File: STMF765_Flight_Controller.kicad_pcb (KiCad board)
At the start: 4 copper layers, 40 x 40 mm, 231 parts, among them J1 10155435-00011LF, SW1 SW_Push, U1 STM32F765VITx, U10 ESDS304DBVR, U11 ESD351DPYR, U12 ATtiny25-20SS, U13 TJA1051TK-3, U14 TJA1051TK-3, U2 AT7456E, U3 TXU0304PWR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

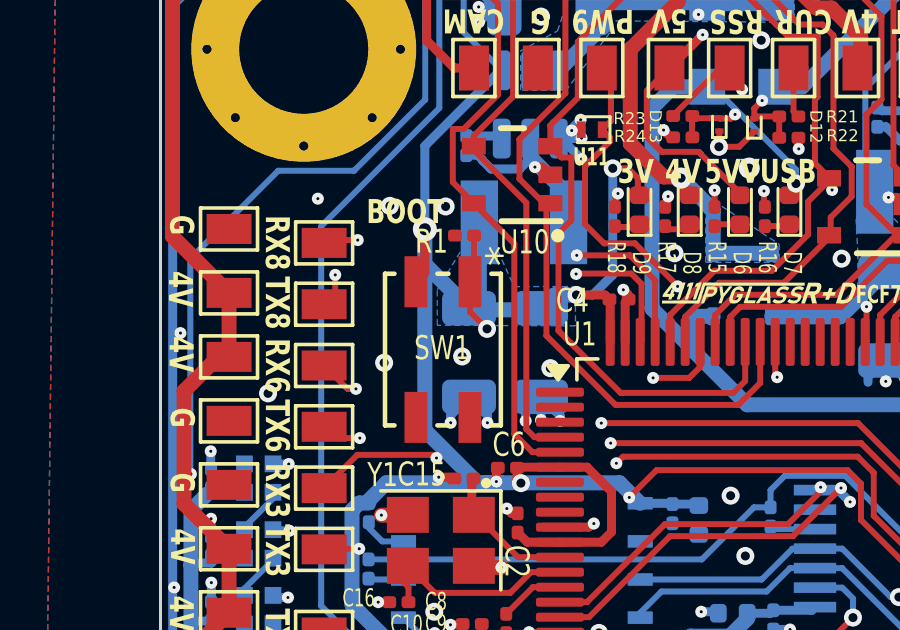
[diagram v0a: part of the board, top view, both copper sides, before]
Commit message: use smaller button
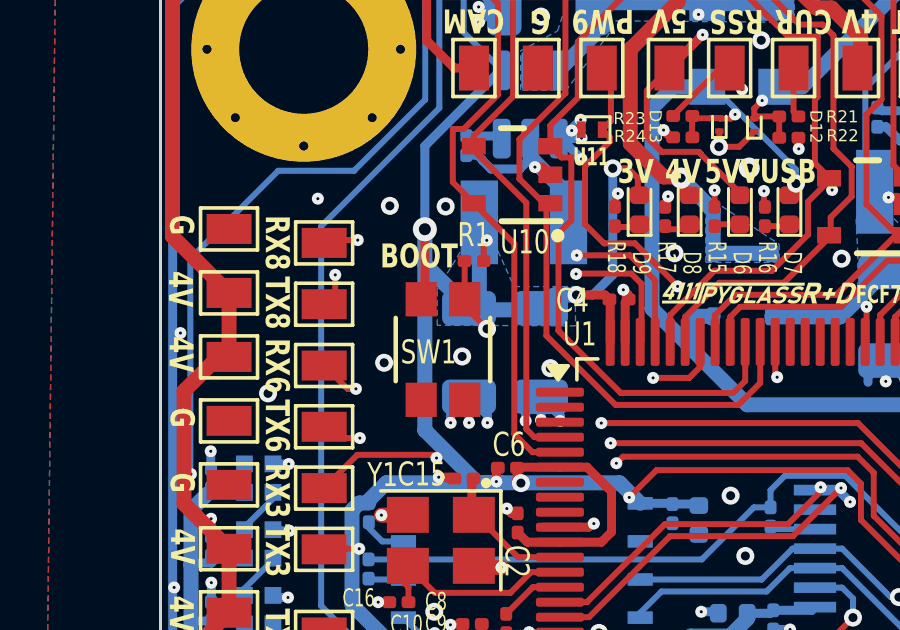
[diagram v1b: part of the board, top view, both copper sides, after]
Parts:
- R15, R16: value 3k3 -> 1k5
- R17: value 3k3 -> 1k2
- R18, R29: value 1k2 -> 680
- R21: value 22k1 -> 0
- R22: value 3k3 -> 10M
- R23: value 3k3 -> 0
- SW1: footprint Project:SWITCH_EVQP2_PAN -> Project:EVPAA602
- moved R1 0.91 mm to (160.3, 62.1), turned to 0 degrees
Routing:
- net Net-(U1-BOOT0): track 12.2 -> 11.3 mm
- net GND: track 116.1 -> 116.8 mm, vias 184 -> 185
- net +3V3: track 355.2 -> 355.7 mm

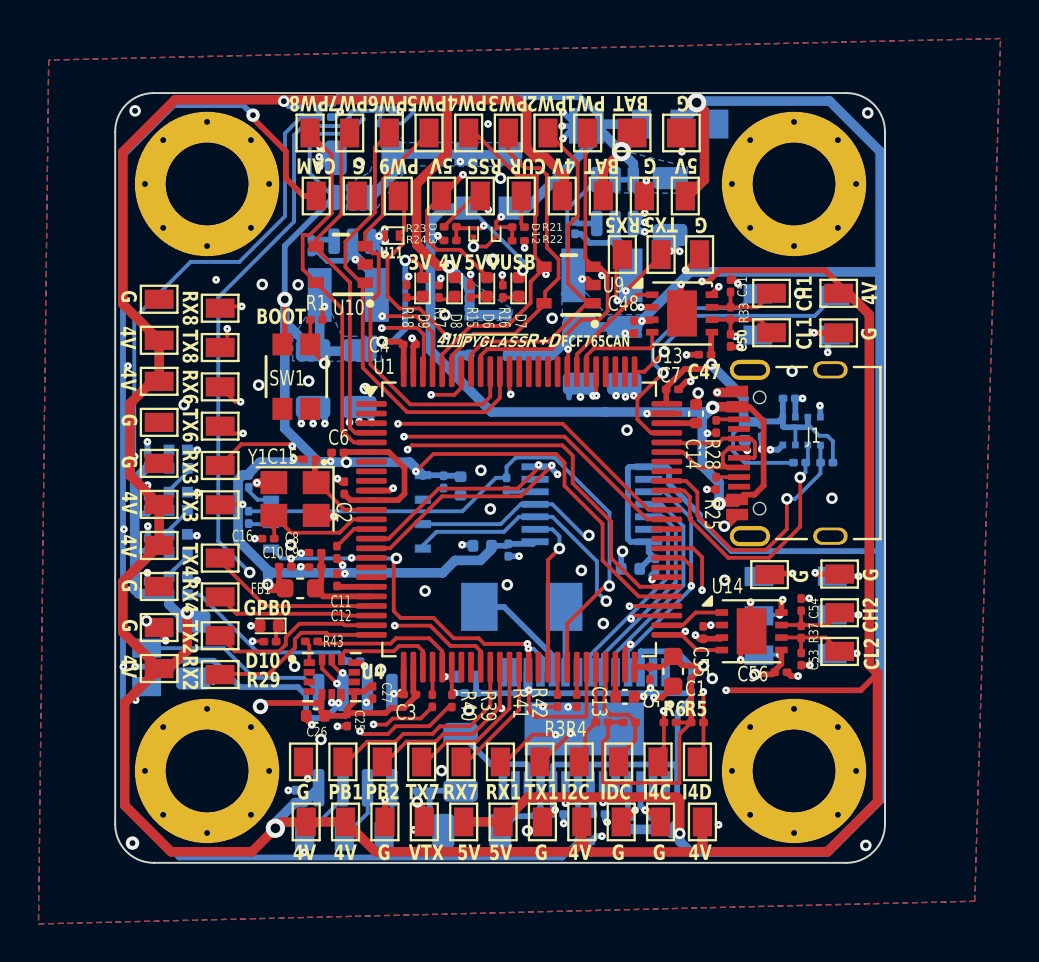
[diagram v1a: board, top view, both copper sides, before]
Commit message: remove microvias, still need to update silkmasks
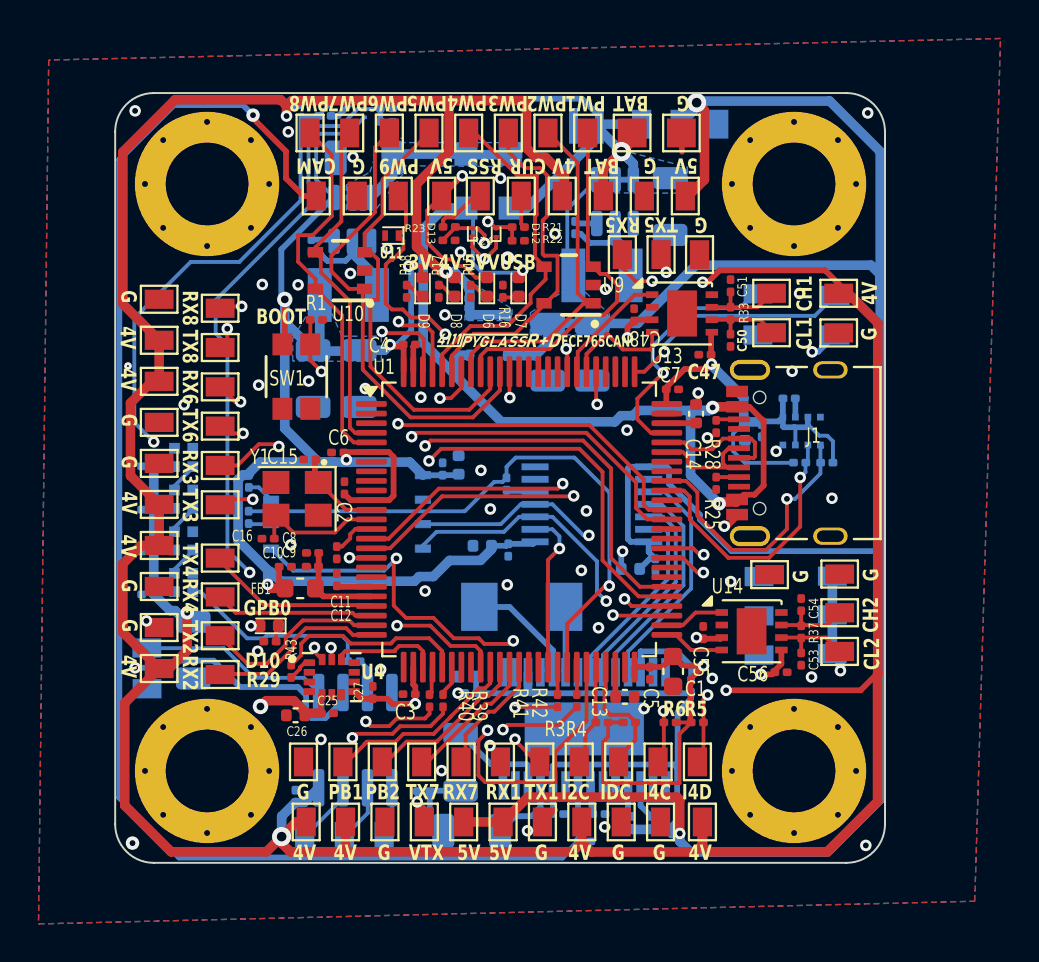
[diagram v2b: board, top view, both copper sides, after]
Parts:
- moved R43 1.88 mm to (159.0, 80.3), turned to 90 degrees
- moved C35 1.69 mm to (172.3, 63.7)
- moved C36 1.68 mm to (174.6, 63.7)
- moved C29 1.09 mm to (167.7, 69.6), turned to 90 degrees
- moved C25 1.09 mm to (160.8, 82.5), turned to 0 degrees
- moved C26 1.03 mm to (159.2, 82.6)
- moved R31 0.81 mm to (160.7, 50.7), turned to 180 degrees
- moved R19 0.78 mm to (163.9, 51.1)
- moved R30 0.68 mm to (160.7, 51.5)
- moved C28 0.67 mm to (166.8, 69.8), turned to 90 degrees
- moved R20 0.65 mm to (163.9, 51.8)
- moved C48 0.64 mm to (176.8, 61.8), turned to -90 degrees
- moved R39 0.46 mm to (166.9, 81.8)
- moved C42 0.36 mm to (151.5, 74.1), turned to 180 degrees
- moved C43 0.36 mm to (151.5, 71.9), turned to 180 degrees
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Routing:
- net GND: track 116.8 -> 22.5 mm, vias 185 -> 51
- net SPI4_CS_FLASH: track 26.3 -> 35.4 mm
- net SPI4_MOSI: track 19.8 -> 27.3 mm
- net +3V3: track 355.7 -> 362.2 mm, vias 14 -> 13
- net ADC1_IN2_RSS: track 28.1 -> 32.7 mm
- net ADC1_IN1_A: track 28.8 -> 33.3 mm
- net +4V: track 208.1 -> 212.6 mm
- net USART1_TX: track 11.3 -> 15.6 mm
- net USART1_RX: track 13.5 -> 16.9 mm
- net VBUS: track 47.0 -> 50.2 mm
- net SPI1_MISO: track 7.73 -> 10.2 mm
- net SPI1_SCK: track 7.97 -> 10.3 mm
- net SPI4_SCK: track 20.4 -> 22.5 mm
- net SPI1_MOSI: track 9.95 -> 11.9 mm
- net UART5_TX: track 10.1 -> 11.8 mm
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
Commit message: adjust silk screens after microvia replacement
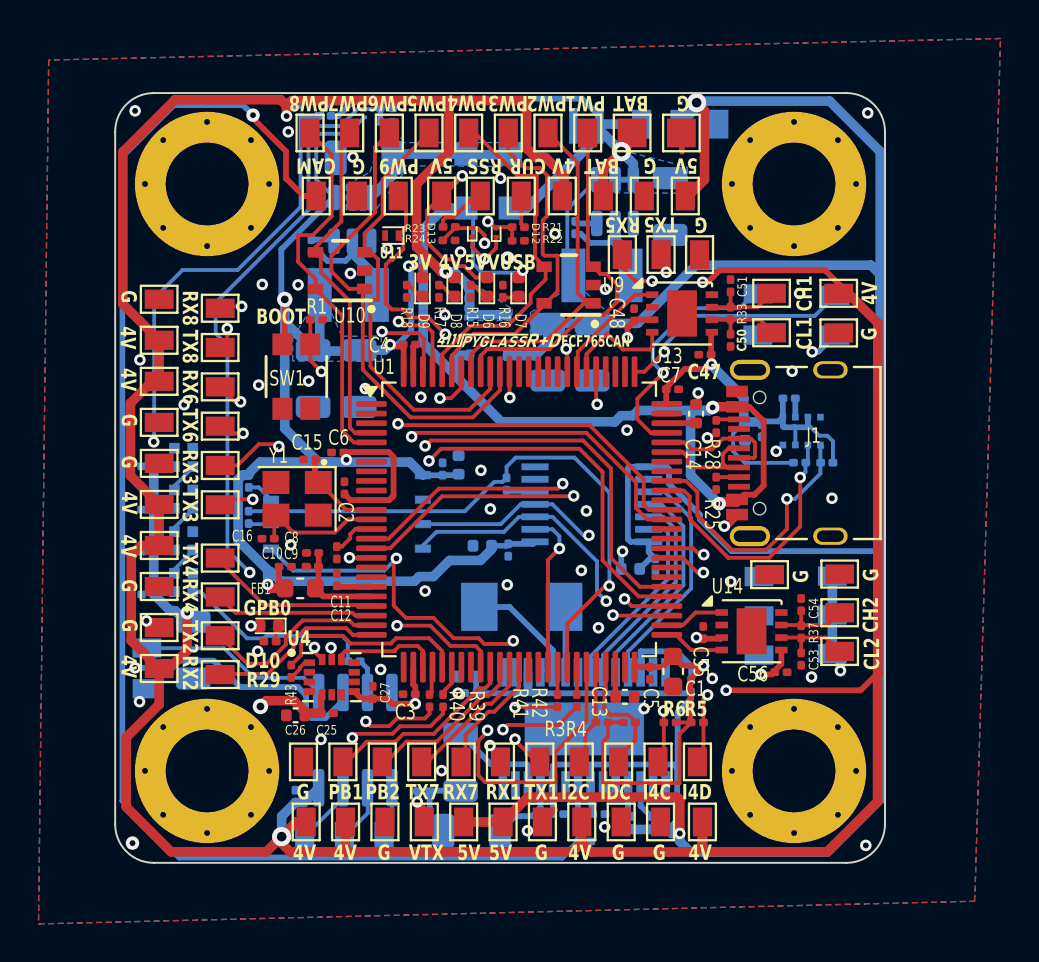
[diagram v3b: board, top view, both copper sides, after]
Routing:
- net /Power Monitor/ADC: track 50.2 -> 49.5 mm
- net GND: vias 51 -> 52

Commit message: change flash to sd flash, cleanup, and reconcile with F405FC
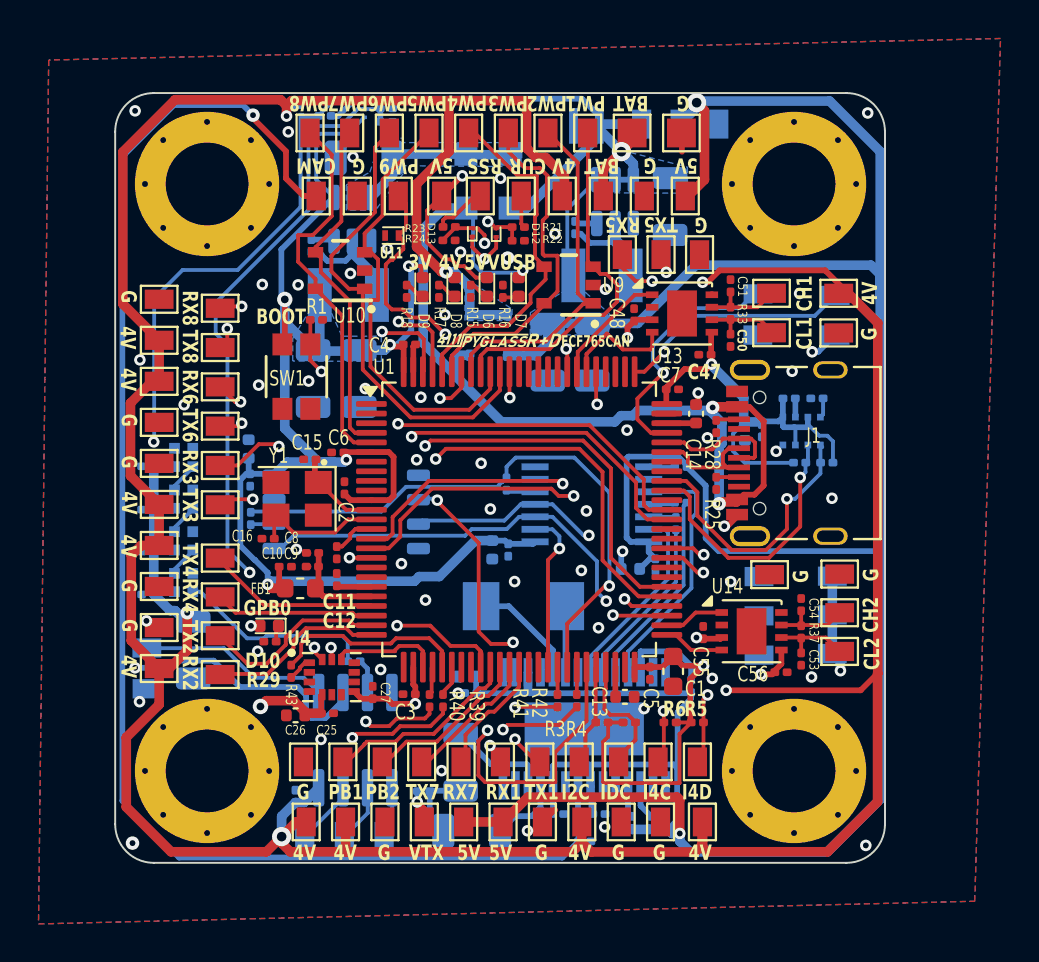
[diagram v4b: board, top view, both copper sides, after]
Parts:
- removed the G*** at (154.2, 64.9)
- removed R14: 5k1, Project:R_0201_0603Metric
- removed R44: 22, Project:R_0201_0603Metric
- added G***: LOGO, Project:4111spyglass15, B.Cu at (161.3, 78.7)
- added G***: LOGO, Project:dronepcb, B.Cu at (152.7, 63.9)
- added R13: 22, Project:R_0201_0603Metric, B.Cu at (179.0, 72.7)
- added R26: 22, Project:R_0201_0603Metric, B.Cu at (179.2, 71.6)
- added R27: 5k1, Project:R_0201_0603Metric, B.Cu at (179.2, 69.7)
- added R34: 100k, Project:R_0201_0603Metric, B.Cu at (186.3, 66.1)
- added R35: 22, Project:R_0201_0603Metric, B.Cu at (156.9, 72.4)
- D10: value YELLOW GPIO -> ORANGE GPIO
- R30: value 20k5 -> 22k1
- R31: value 4k99 -> 5k36
- U5: value MT29F2G01ABAGDWB-IT_G -> XTSD04G; footprint Project:SON127P600X800X65-8N -> Package_LGA:LGA-8_8x6mm_P1.27mm
- moved C29 10.9 mm to (156.8, 68.8)
- moved C28 10.0 mm to (156.8, 70.4), turned to -90 degrees
- moved C52 0.56 mm to (169.4, 74.0), turned to -90 degrees
- moved Y2 0.09 mm to (171.0, 76.9)
- turned U5 to 180 degrees
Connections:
- net Net-(U2-CLKIN) renamed /Peripherals/CLKIN
- net Net-(U2-XFB) renamed /Peripherals/XFB
- U3 pad 11: /Peripherals/SPI4_SCK_4V -> Net-(U3-B3Y)
- U3 pad 12: /Peripherals/SPI4_MOSI_4V -> Net-(U3-B2Y)
- U3 pad 8: +5V -> Net-(U3-OE)
- U5 pad 1: SPI4_CS_FLASH -> unconnected-(U5-SD2-Pad1)
- U5 pad 2: Net-(U5-SO/IO1) -> SPI4_CS_FLASH
- U5 pad 3: Net-(U5-WP/IO2) -> SPI4_SCK
- U5 pad 5: +3V3 -> SPI4_MOSI
- U5 pad 6: unconnected-(U5-HOLD/IO3-Pad6) -> Net-(U5-SD0/DO)
- U5 pad 7: SPI4_SCK -> unconnected-(U5-SD1-Pad7)
- U5 pad 8: SPI4_MOSI -> +3V3
- U6 pad 5: GND -> Net-(U6-SDO)
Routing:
- net SPI4_MOSI: track 27.3 -> 34.8 mm
- net SPI4_CS_FLASH: track 35.4 -> 29.3 mm
- net +3V3: track 362.2 -> 356.1 mm
- net +5V: track 190.1 -> 191.8 mm
- net /Peripherals/SPI4_MOSI_4V: track 10.7 -> 8.97 mm
- net Net-(U3-B2Y): track 0.00 -> 1.50 mm
- net Net-(U3-OE): track 0.00 -> 1.46 mm
- net Net-(U5-WP/IO2): track 1.42 -> 0.00 mm
- net Net-(U3-B3Y): track 0.00 -> 1.38 mm
- net VBUS: track 50.2 -> 48.9 mm
- net Net-(U5-SD0/DO): track 0.00 -> 1.22 mm
- net Net-(U5-SO/IO1): track 1.16 -> 0.00 mm
- net /Peripherals/SPI4_MISO_4V: track 12.1 -> 13.3 mm
- net Net-(U6-SDO): track 0.00 -> 1.03 mm
- net /Peripherals/SPI4_SCK_4V: track 11.4 -> 10.4 mm
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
